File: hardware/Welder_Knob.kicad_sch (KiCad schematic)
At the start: 25 parts, among them IC1 ESP32-C3-MINI-1-N4, J3 UART, J7 Power, J9 Motor_Header, SW1 Reset, SW2 General Input

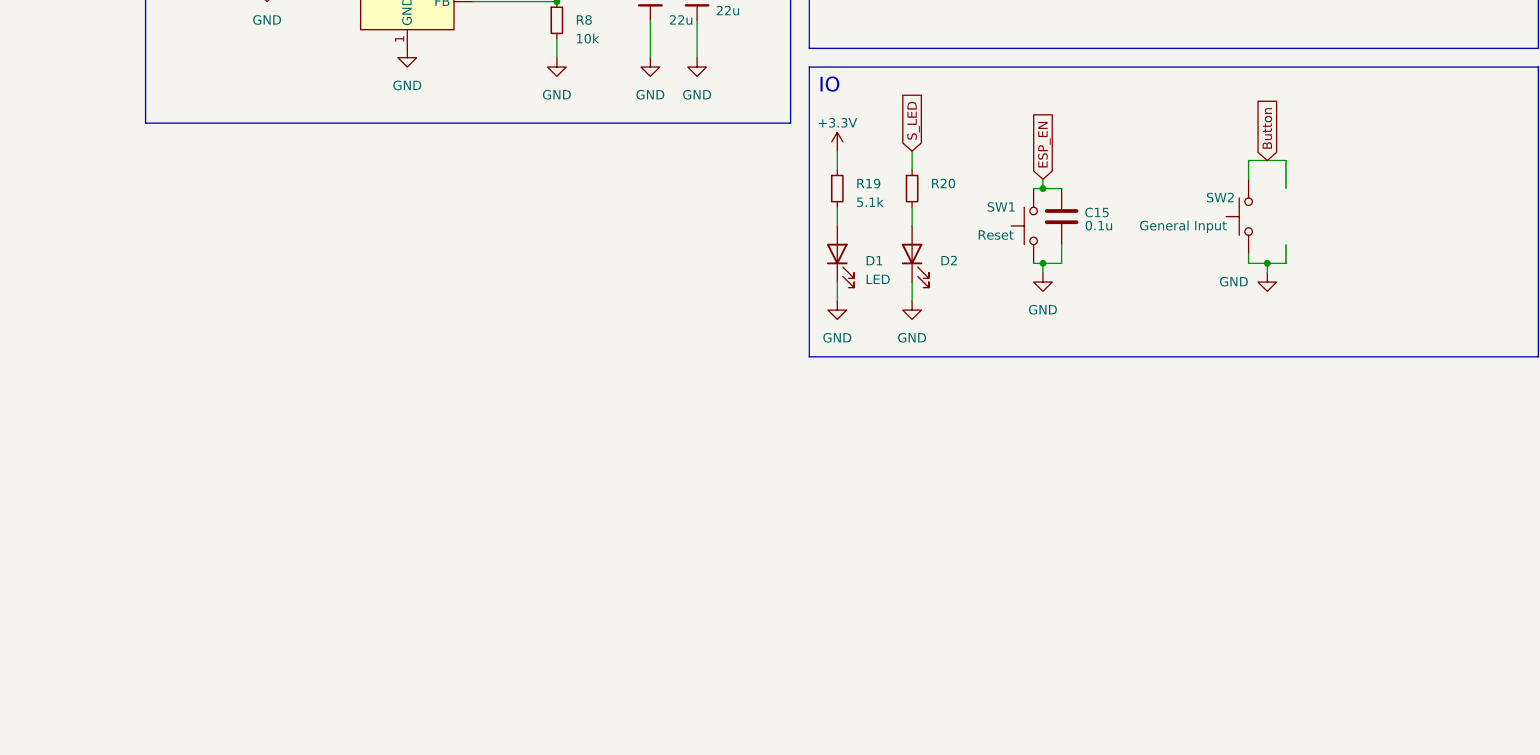
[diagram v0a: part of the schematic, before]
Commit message: Completed Power Path
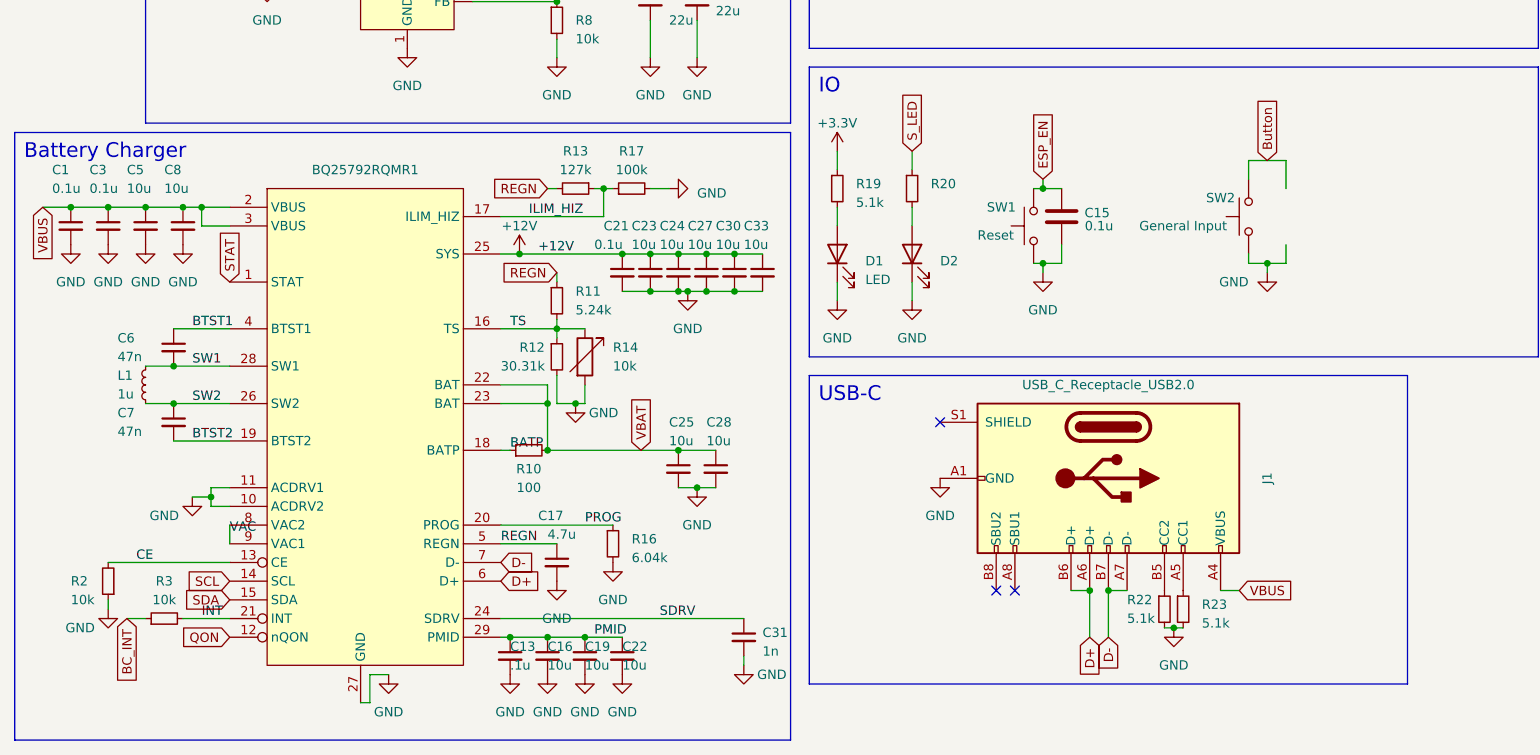
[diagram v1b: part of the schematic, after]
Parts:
- added BQ25792RQMR1: ~, Lipo_Charger:BQ25792, symbol LiPo_Charger_BQ25792RQMR:BQ25792RQMR
- added C1, C21, C3: 0.1u, Capacitor_SMD:C_0402_1005Metric, symbol Device:C_Small
- added C13: .1u, Capacitor_SMD:C_0402_1005Metric, symbol Device:C_Small
- added C16, C19, C22, C23, C24, C25, C27, C28, C30, C33, C5, C8: 10u, Capacitor_SMD:C_0603_1608Metric, symbol Device:C_Small
- added C17: 4.7u, Capacitor_SMD:C_0402_1005Metric, symbol Device:C_Small
- added C31: 1n, Capacitor_SMD:C_0402_1005Metric, symbol Device:C_Small
- added C6, C7: 47n, Capacitor_SMD:C_0402_1005Metric, symbol Device:C_Small
- added J1: USB_C_Receptacle_USB2.0, Connector_USB:USB_C_Receptacle_JAE_DX07S016JA1R1500, symbol Connector:USB_C_Receptacle_USB2.0
- added L1: 1u, Inductor_SMD:L_Sunlord_MWSA0402S, symbol Device:L_Small
- added R10: 100, Resistor_SMD:R_0402_1005Metric, symbol Device:R_Small
- added R11: 5.24k, Resistor_SMD:R_0402_1005Metric, symbol Device:R_Small
- added R12: 30.31k, Resistor_SMD:R_0402_1005Metric, symbol Device:R_Small
- added R13: 127k, Resistor_SMD:R_0402_1005Metric, symbol Device:R_Small
- added R14: 10k, Resistor_SMD:R_0402_1005Metric, symbol Device:R_Variable
- added R16: 6.04k, Resistor_SMD:R_0402_1005Metric, symbol Device:R_Small
- added R17: 100k, Resistor_SMD:R_0402_1005Metric, symbol Device:R_Small
- added R2, R3: 10k, Resistor_SMD:R_0402_1005Metric, symbol Device:R_Small
- added R22, R23: 5.1k, Resistor_SMD:R_0402_1005Metric, symbol Device:R_Small
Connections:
- net +12V: now also BQ25792RQMR1.25 (SYS), C21.1, C23.1, C24.1, C27.1, C30.1, C33.1
- net GND: now also BQ25792RQMR1.10 (ACDRV2), BQ25792RQMR1.11 (ACDRV1), BQ25792RQMR1.27 (GND), C1.2, C13.2, C16.2, C17.2, C19.2, C21.2, C22.2, C23.2, C24.2, C25.2, C27.2, C28.2, C3.2, C30.2, C31.2, C33.2, C5.2, C8.2, J1.A1 (GND), J1.A12 (GND), J1.B1 (GND), J1.B12 (GND), R12.2, R14.2, R16.2, R17.2, R2.1, R22.2, R23.2
- new net: J1.A5 (CC1), R23.1
- new net: J1.B5 (CC2), R22.1
- new net BATP: BQ25792RQMR1.18 (BATP), R10.1
- new net BC_INT: R3.1
- new net BTST1: BQ25792RQMR1.4 (BTST1), C6.1
- new net BTST2: BQ25792RQMR1.19 (BTST2), C7.2
- new net CE: BQ25792RQMR1.13 (CE), R2.2
- new net D+: BQ25792RQMR1.6 (D+), J1.A6 (D+), J1.B6 (D+)
- new net D-: BQ25792RQMR1.7 (D-), J1.A7 (D-), J1.B7 (D-)
- new net ILIM_HIZ: BQ25792RQMR1.17 (ILIM_HIZ), R13.1, R17.1
- new net INT: BQ25792RQMR1.21 (INT), R3.2
- new net PMID: BQ25792RQMR1.29 (PMID), C13.1, C16.1, C19.1, C22.1
- new net PROG: BQ25792RQMR1.20 (PROG), R16.1
- new net QON: BQ25792RQMR1.12 (nQON)
- new net REGN: BQ25792RQMR1.5 (REGN), C17.1, R11.1, R13.2
- new net SCL: BQ25792RQMR1.14 (SCL)
- new net SDA: BQ25792RQMR1.15 (SDA)
- new net SDRV: BQ25792RQMR1.24 (SDRV), C31.1
- new net STAT: BQ25792RQMR1.1 (STAT)
- new net SW1: BQ25792RQMR1.28 (SW1), C6.2, L1.2
- new net SW2: BQ25792RQMR1.26 (SW2), C7.1, L1.1
- new net TS: BQ25792RQMR1.16 (TS), R11.2, R12.1, R14.1
- new net VAC: BQ25792RQMR1.8 (VAC2), BQ25792RQMR1.9 (VAC1)
- new net VBAT: BQ25792RQMR1.22 (BAT), BQ25792RQMR1.23 (BAT), C25.1, C28.1, R10.2
- new net VBUS: BQ25792RQMR1.2 (VBUS), BQ25792RQMR1.3 (VBUS), C1.1, C3.1, C5.1, C8.1, J1.A4 (VBUS), J1.A9 (VBUS), J1.B4 (VBUS), J1.B9 (VBUS)
- no-connect marks 18 -> 21
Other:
- note added: "Battery Charger"
- note added: "USB-C"
